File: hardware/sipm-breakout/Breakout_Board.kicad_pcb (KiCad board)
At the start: 2 copper layers, 14 parts, among them J1 Conn_02x34_Odd_Even, J10 Conn_Coaxial, J11 Conn_Coaxial, J12 Conn_Coaxial, J13 Conn_Coaxial, J14 Conn_Coaxial, J2 Conn_02x34_Odd_Even, J3 Conn_02x30_Odd_Even, J4 Conn_02x30_Odd_Even, J5 Conn_02x04_Top_Bottom, J6 Conn_01x04, J7 Conn_Coaxial, J8 Conn_Coaxial, J9 Conn_Coaxial

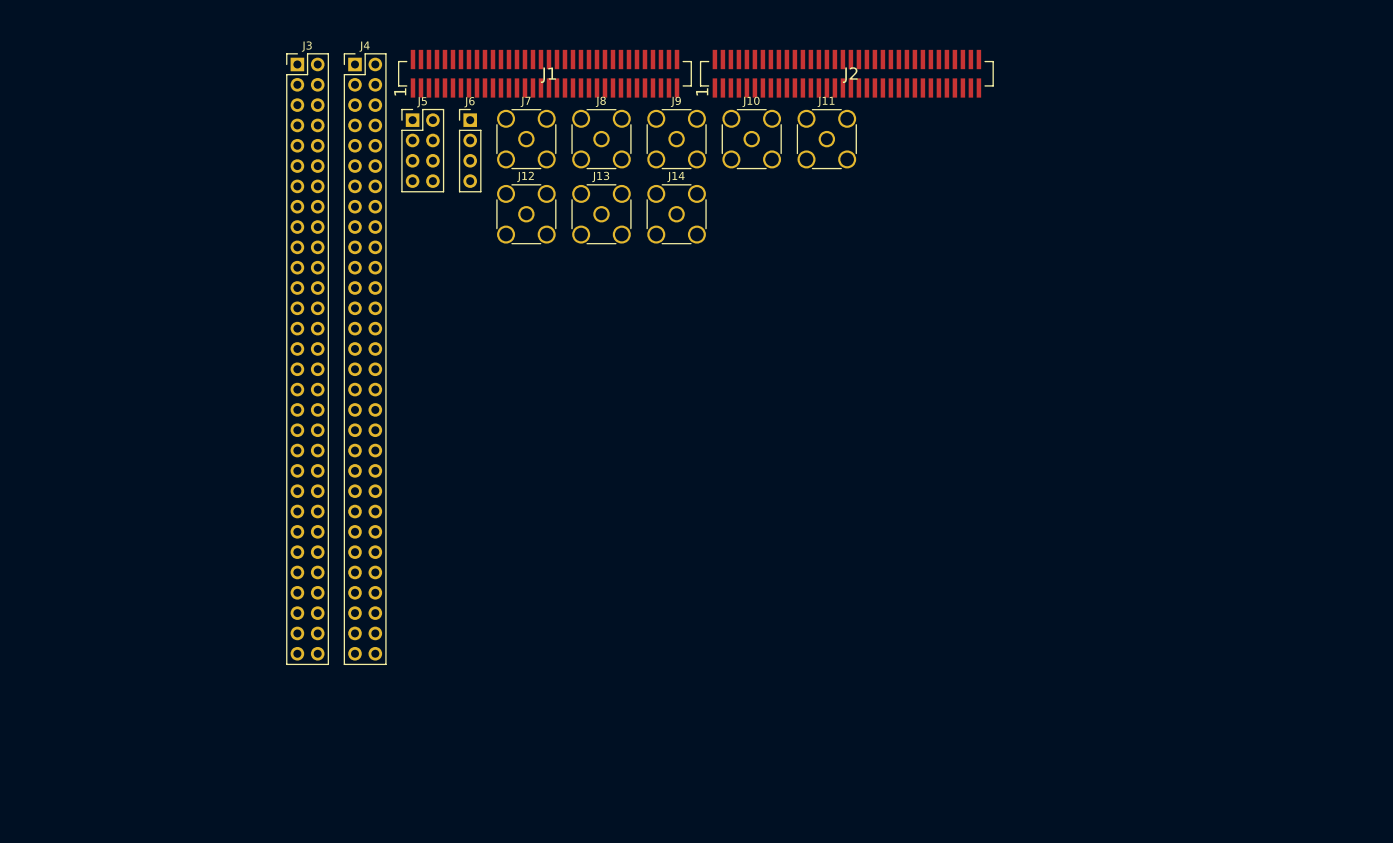
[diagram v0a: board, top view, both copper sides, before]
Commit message: add resistor packs, fix netlist
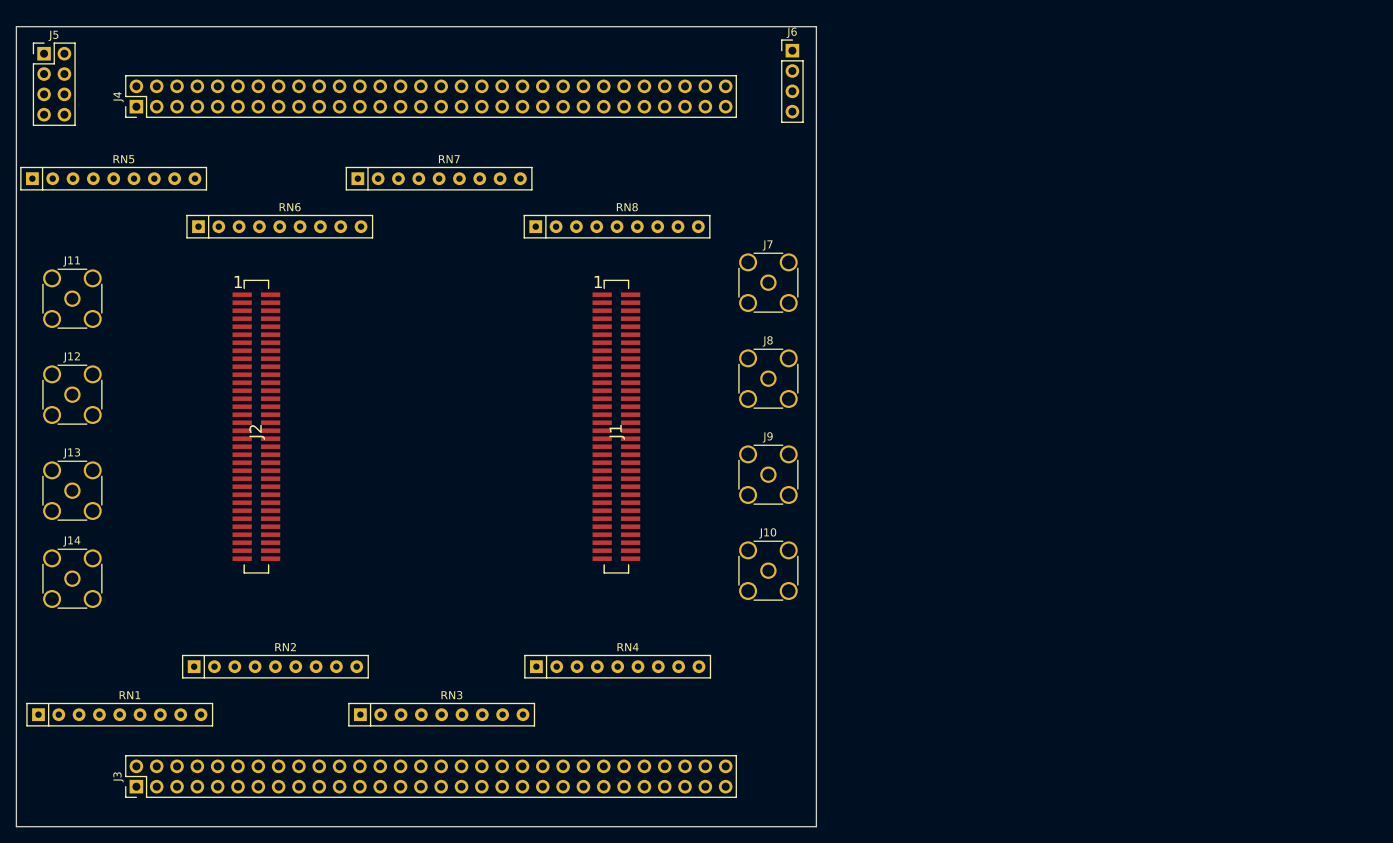
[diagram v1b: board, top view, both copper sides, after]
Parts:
- added RN1: R_Network08_US, Resistor_THT:R_Array_SIP9, F.Cu at (32.8, 111.0)
- added RN2: R_Network08_US, Resistor_THT:R_Array_SIP9, F.Cu at (52.2, 105.0)
- added RN3: R_Network08_US, Resistor_THT:R_Array_SIP9, F.Cu at (73.0, 111.0)
- added RN4: R_Network08_US, Resistor_THT:R_Array_SIP9, F.Cu at (95.0, 105.0)
- added RN5: R_Network08_US, Resistor_THT:R_Array_SIP9, F.Cu at (32.0, 44.0)
- added RN6: R_Network08_US, Resistor_THT:R_Array_SIP9, F.Cu at (52.8, 50.0)
- added RN7: R_Network08_US, Resistor_THT:R_Array_SIP9, F.Cu at (72.7, 44.0)
- added RN8: R_Network08_US, Resistor_THT:R_Array_SIP9, F.Cu at (94.9, 50.0)
- moved J11 96.4 mm to (37.0, 59.0)
- moved J3 92.5 mm to (45.0, 120.0), turned to 90 degrees
- moved J14 88.2 mm to (37.0, 94.0)
- moved J2 86.0 mm to (60.0, 75.0), turned to 270 degrees
- moved J13 74.6 mm to (37.0, 83.0)
- moved J12 61.1 mm to (37.0, 71.0)
- moved J10 54.0 mm to (124.0, 93.0)
- moved J5 46.8 mm to (33.5, 28.4)
- moved J1 45.0 mm to (105.0, 75.0), turned to 270 degrees
- moved J9 43.5 mm to (124.0, 81.0)
- moved J6 41.2 mm to (127.0, 28.0)
- moved J8 36.5 mm to (124.0, 69.0)
- moved J7 35.2 mm to (124.0, 57.0)
- moved J4 27.8 mm to (45.0, 35.0), turned to 90 degrees
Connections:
- J11 pad 1: /CH3 -> /BCH3
- J12 pad 1: /CH2 -> /BCH2
- J13 pad 1: /CH1 -> /BCH1
- J14 pad 1: /CH0 -> /BCH0
- J2 pad 1: /CH0 -> /BCH0
- J2 pad 11: /CH5 -> /BCH5
- J2 pad 13: /CH6 -> /BCH6
- J2 pad 15: /CH7 -> /BCH7
- J2 pad 17: /CH8 -> /BCH8
- J2 pad 19: /CH9 -> /BCH9
- J2 pad 21: /CH10 -> /BCH10
- J2 pad 23: /CH11 -> /BCH11
- J2 pad 25: /CH12 -> /BCH12
- J2 pad 27: /CH13 -> /BCH13
- J2 pad 29: /CH14 -> /BCH14
- J2 pad 3: /CH1 -> /BCH1
- J2 pad 31: /CH15 -> /BCH15
- J2 pad 33: /CH16 -> /BCH16
- J2 pad 35: /CH17 -> /BCH17
- J2 pad 37: /CH18 -> /BCH18
- J2 pad 39: /CH19 -> /BCH19
- J2 pad 41: /CH20 -> /BCH20
- J2 pad 43: /CH21 -> /BCH21
- J2 pad 45: /CH22 -> /BCH22
- J2 pad 47: /CH23 -> /BCH23
- J2 pad 49: /CH24 -> /BCH24
- J2 pad 5: /CH2 -> /BCH2
- J2 pad 51: /CH25 -> /BCH25
- J2 pad 53: /CH26 -> /BCH26
- J2 pad 55: /CH27 -> /BCH27
- J2 pad 57: /CH28 -> /BCH28
- J2 pad 59: /CH29 -> /BCH29
- J2 pad 61: /CH30 -> /BCH30
- J2 pad 63: /CH31 -> /BCH31
- J2 pad 7: /CH3 -> /BCH3
- J2 pad 9: /CH4 -> /BCH4
- J4 pad 1: /CH4 -> /BCH4
- J4 pad 11: /CH9 -> /BCH9
- J4 pad 13: /CH10 -> /BCH10
- J4 pad 15: /CH11 -> /BCH11
- J4 pad 17: /CH12 -> /BCH12
- J4 pad 19: /CH13 -> /BCH13
- J4 pad 21: /CH14 -> /BCH14
- J4 pad 23: /CH15 -> /BCH15
- J4 pad 25: /CH16 -> /BCH16
- J4 pad 27: /CH17 -> /BCH17
- J4 pad 29: /CH18 -> /BCH18
- J4 pad 3: /CH5 -> /BCH5
- J4 pad 31: /CH19 -> /BCH19
- J4 pad 33: /CH20 -> /BCH20
- J4 pad 35: /CH21 -> /BCH21
- J4 pad 37: /CH22 -> /BCH22
- J4 pad 39: /CH23 -> /BCH23
- J4 pad 41: /CH24 -> /BCH24
- J4 pad 43: /CH25 -> /BCH25
- J4 pad 45: /CH26 -> /BCH26
- J4 pad 47: /CH27 -> /BCH27
- J4 pad 49: /CH28 -> /BCH28
- J4 pad 5: /CH6 -> /BCH6
- J4 pad 51: /CH29 -> /BCH29
- J4 pad 53: /CH30 -> /BCH30
- J4 pad 55: /CH31 -> /BCH31
- J4 pad 7: /CH7 -> /BCH7
- J4 pad 9: /CH8 -> /BCH8
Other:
- board outline added: 100 x 100 mm

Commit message: partially routed
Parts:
- added H1: MountingHole_Pad, MountingHole:MountingHole_4.3mm_M4_Pad, F.Cu at (105.0, 30.0)
- added H2: MountingHole_Pad, MountingHole:MountingHole_4.3mm_M4_Pad, F.Cu at (105.0, 120.0)
- added H3: MountingHole_Pad, MountingHole:MountingHole_4.3mm_M4_Pad, F.Cu at (195.0, 30.0)
- added H4: MountingHole_Pad, MountingHole:MountingHole_4.3mm_M4_Pad, F.Cu at (195.0, 120.0)
- J1, J2: footprint Arich_SiPM_Footprints:MW-34-03-G-D-245-065-ES -> Breakout_Board_Parts:SAMTEC_CLM-134-02-F-D
- J10, J11, J12, J13, J14, J7, J8, J9: footprint Connector_Coaxial:SMA_Amphenol_132134_Vertical -> Breakout_Board_Parts:lemo-EPB.00.250.NTN
- J3, J4: value Conn_02x30_Odd_Even -> Conn_02x32_Odd_Even; footprint Connector_PinHeader_2.54mm:PinHeader_2x30_P2.54mm_Vertical -> Connector_PinHeader_2.00mm:PinHeader_2x32_P2.00mm_Vertical_SMD; moved to B.Cu
- RN1, RN2, RN3, RN4, RN5, RN6, RN7, RN8: footprint Resistor_THT:R_Array_SIP9 -> Breakout_Board_Parts:RPKG-9; moved to B.Cu
- moved J14 166.3 mm to (195.0, 42.0)
- moved J13 161.4 mm to (195.0, 50.0)
- moved J12 158.5 mm to (195.0, 58.0)
- moved J11 158.2 mm to (195.0, 66.0)
- moved RN5 154.1 mm to (186.0, 50.7), turned to 270 degrees
- moved J5 149.6 mm to (151.6, 120.1), turned to 90 degrees
- moved J4 137.0 mm to (176.0, 75.0), turned to 180 degrees
- moved RN6 134.3 mm to (186.0, 67.0), turned to 270 degrees
- moved RN7 119.8 mm to (186.0, 83.0), turned to 270 degrees
- moved J2 105.6 mm to (164.2, 58.0), turned to 90 degrees
- moved RN8 103.0 mm to (186.0, 98.0), turned to 270 degrees
- moved RN1 101.8 mm to (115.0, 51.0), turned to 270 degrees
- moved J6 92.0 mm to (122.1, 119.8), turned to 90 degrees
- moved J3 91.3 mm to (125.0, 76.0), turned to 180 degrees
- moved RN2 73.9 mm to (115.0, 66.0), turned to 270 degrees
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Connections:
- J3 pad 1: /CH4 -> /CH0
- J3 pad 11: /CH9 -> /CH5
- J3 pad 13: /CH10 -> /CH6
- J3 pad 15: /CH11 -> /CH7
- J3 pad 17: /CH12 -> /CH8
- J3 pad 19: /CH13 -> /CH9
- J3 pad 21: /CH14 -> /CH10
- J3 pad 23: /CH15 -> /CH11
- J3 pad 25: /CH16 -> /CH12
- J3 pad 27: /CH17 -> /CH13
- J3 pad 29: /CH18 -> /CH14
- J3 pad 3: /CH5 -> /CH1
- J3 pad 31: /CH19 -> /CH15
- J3 pad 33: /CH20 -> /CH16
- J3 pad 35: /CH21 -> /CH17
- J3 pad 37: /CH22 -> /CH18
- J3 pad 39: /CH23 -> /CH19
- J3 pad 41: /CH24 -> /CH20
- J3 pad 43: /CH25 -> /CH21
- J3 pad 45: /CH26 -> /CH22
- J3 pad 47: /CH27 -> /CH23
- J3 pad 49: /CH28 -> /CH24
- J3 pad 5: /CH6 -> /CH2
- J3 pad 51: /CH29 -> /CH25
- J3 pad 53: /CH30 -> /CH26
- J3 pad 55: /CH31 -> /CH27
- J3 pad 57: Net-(J3-Pad57) -> /CH28
- J3 pad 59: Net-(J3-Pad59) -> /CH29
- J3 pad 7: /CH7 -> /CH3
- J3 pad 9: /CH8 -> /CH4
- J4 pad 1: /BCH4 -> /BCH0
- J4 pad 11: /BCH9 -> /BCH5
- J4 pad 13: /BCH10 -> /BCH6
- J4 pad 15: /BCH11 -> /BCH7
- J4 pad 17: /BCH12 -> /BCH8
- J4 pad 19: /BCH13 -> /BCH9
- J4 pad 21: /BCH14 -> /BCH10
- J4 pad 23: /BCH15 -> /BCH11
- J4 pad 25: /BCH16 -> /BCH12
- J4 pad 27: /BCH17 -> /BCH13
- J4 pad 29: /BCH18 -> /BCH14
- J4 pad 3: /BCH5 -> /BCH1
- J4 pad 31: /BCH19 -> /BCH15
- J4 pad 33: /BCH20 -> /BCH16
- J4 pad 35: /BCH21 -> /BCH17
- J4 pad 37: /BCH22 -> /BCH18
- J4 pad 39: /BCH23 -> /BCH19
- J4 pad 41: /BCH24 -> /BCH20
- J4 pad 43: /BCH25 -> /BCH21
- J4 pad 45: /BCH26 -> /BCH22
- J4 pad 47: /BCH27 -> /BCH23
- J4 pad 49: /BCH28 -> /BCH24
- J4 pad 5: /BCH6 -> /BCH2
- J4 pad 51: /BCH29 -> /BCH25
- J4 pad 53: /BCH30 -> /BCH26
- J4 pad 55: /BCH31 -> /BCH27
- J4 pad 57: Net-(J4-Pad57) -> /BCH28
- J4 pad 59: Net-(J4-Pad59) -> /BCH29
- J4 pad 7: /BCH7 -> /BCH3
- J4 pad 9: /BCH8 -> /BCH4
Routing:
- net GND: track 0.00 -> 83.8 mm, vias 0 -> 43
- net /CH3: track 0.00 -> 55.1 mm, vias 0 -> 1
- net /CH2: track 0.00 -> 48.3 mm, vias 0 -> 1
- net /CH0: track 0.00 -> 47.7 mm, vias 0 -> 1
- net /CH1: track 0.00 -> 43.5 mm, vias 0 -> 1
- net /CH23: track 0.00 -> 31.5 mm, vias 0 -> 1
- net /CH4: track 0.00 -> 31.2 mm, vias 0 -> 1
- net /CH5: track 0.00 -> 31.0 mm, vias 0 -> 1
- net /CH6: track 0.00 -> 30.1 mm, vias 0 -> 1
- net /CH22: track 0.00 -> 29.9 mm, vias 0 -> 1
- net /CH7: track 0.00 -> 28.6 mm, vias 0 -> 1
- net /CH31: track 0.00 -> 28.0 mm, vias 0 -> 1
- net /CH20: track 0.00 -> 28.0 mm, vias 0 -> 1
- net /CH15: track 0.00 -> 27.7 mm, vias 0 -> 1
- net /BCH0: track 0.00 -> 27.5 mm, vias 0 -> 1
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- added copper zone on F.Cu, net GND
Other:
- net class Default: clearance 0.2 -> 0.1778; trace_width 0.25 -> 0.1778; via_dia 0.8 -> 0.635; via_drill 0.4 -> 0.3048
- rule pad_to_mask_clearance: 0 -> 0.0381
- rule trace_clearance: 0.2 -> 0.1778
- rule trace_min: 0.2 -> 0.1778
- rule via_min_drill: 0.3 -> 0.2032
- rule via_min_size: 0.4 -> 0.635

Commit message: Possibly final break board
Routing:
- net /BIAS1: track 0.00 -> 82.5 mm, vias 0 -> 4
- net /BIAS3: track 0.00 -> 71.3 mm, vias 0 -> 4
- net GND: track 83.8 -> 135.5 mm, vias 43 -> 71
- net /VDD: track 0.00 -> 47.4 mm, vias 0 -> 1
- net /BCH31: track 0.00 -> 41.9 mm, vias 0 -> 1
- net /OUT: track 0.00 -> 41.2 mm, vias 0 -> 1
- net /BCH30: track 0.00 -> 41.0 mm, vias 0 -> 1
- net /BCH29: track 0.00 -> 39.2 mm, vias 0 -> 1
- net /BCH28: track 0.00 -> 38.5 mm, vias 0 -> 1
- net /BIAS2: track 0.00 -> 37.2 mm, vias 0 -> 1
- net /BCH27: track 0.00 -> 37.2 mm, vias 0 -> 1
- net /BCH26: track 0.00 -> 35.7 mm, vias 0 -> 1
- net /BCH25: track 0.00 -> 34.9 mm, vias 0 -> 1
- net /BCH24: track 0.00 -> 34.4 mm, vias 0 -> 1
- net /BIAS4: track 0.00 -> 33.7 mm
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- added copper zone on B.Cu, net GND
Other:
- board text added: "EMPHATIC SiPM Breakout Rev A -- 2021-03 ESH http://edf.bu.edu"
- board text added: "UP"

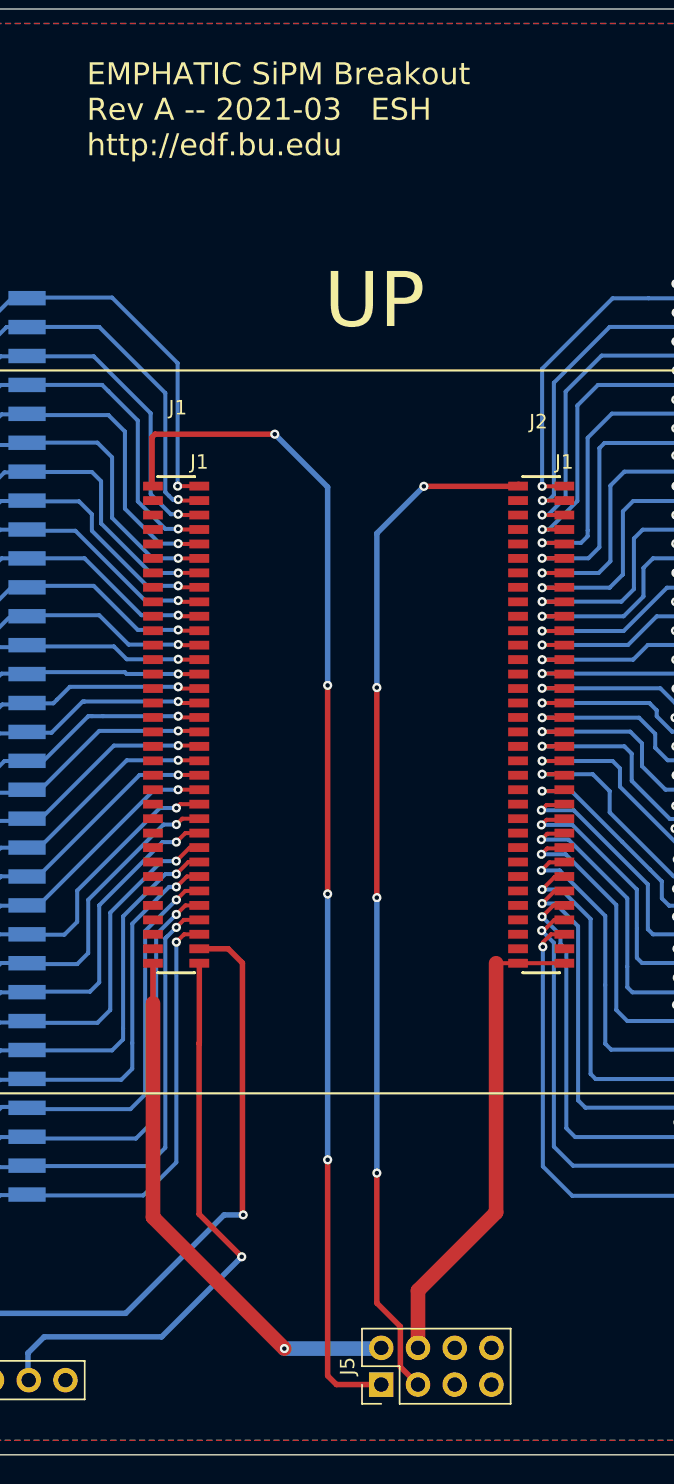
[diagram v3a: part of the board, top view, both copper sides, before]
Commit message: Rev B breakout board
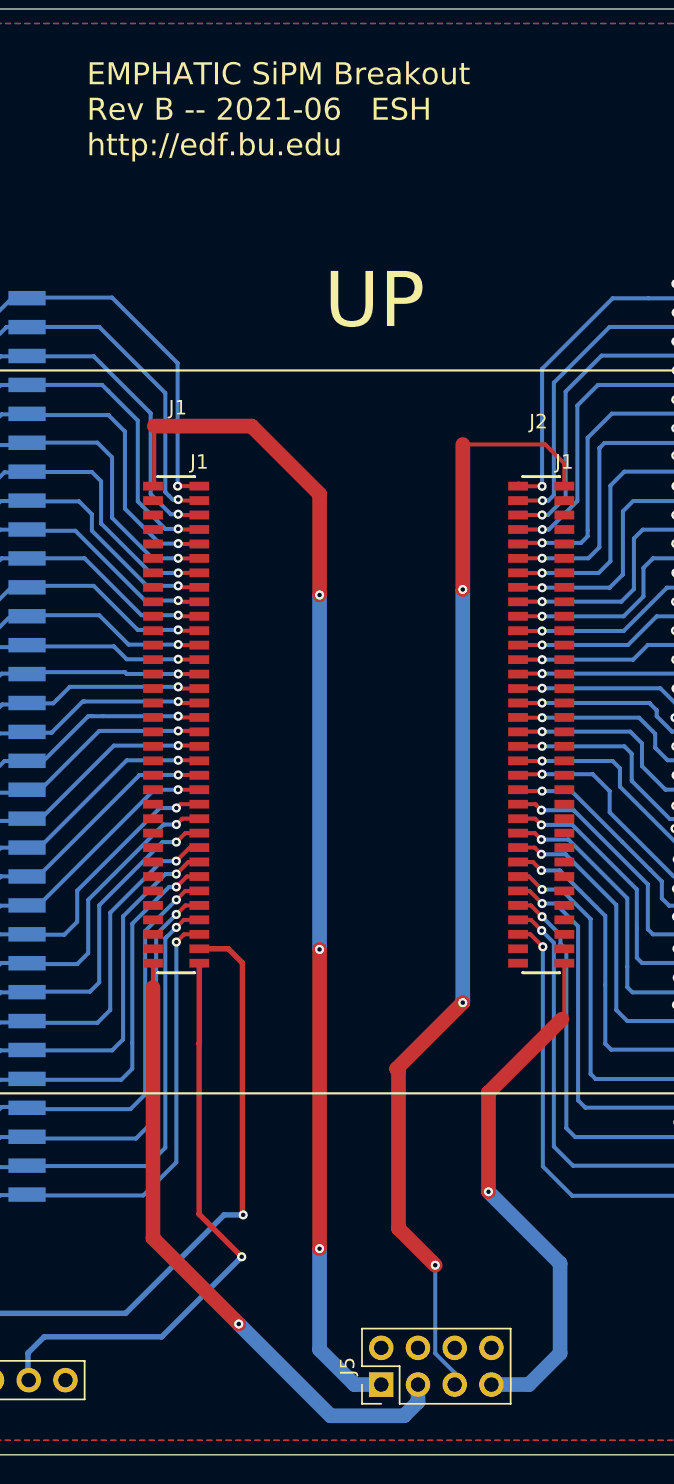
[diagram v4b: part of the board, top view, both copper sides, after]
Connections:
- J2 pad 1: /BCH0 -> /BIAS3
- J2 pad 10: GND -> /BCH4
- J2 pad 11: /BCH5 -> GND
- J2 pad 12: GND -> /BCH5
- J2 pad 13: /BCH6 -> GND
- J2 pad 14: GND -> /BCH6
- J2 pad 15: /BCH7 -> GND
- J2 pad 16: GND -> /BCH7
- J2 pad 17: /BCH8 -> GND
- J2 pad 18: GND -> /BCH8
- J2 pad 19: /BCH9 -> GND
- J2 pad 2: /BIAS3 -> /BCH0
- J2 pad 20: GND -> /BCH9
- J2 pad 21: /BCH10 -> GND
- J2 pad 22: GND -> /BCH10
- J2 pad 23: /BCH11 -> GND
- J2 pad 24: GND -> /BCH11
- J2 pad 25: /BCH12 -> GND
- J2 pad 26: GND -> /BCH12
- J2 pad 27: /BCH13 -> GND
- J2 pad 28: GND -> /BCH13
- J2 pad 29: /BCH14 -> GND
- J2 pad 3: /BCH1 -> GND
- J2 pad 30: GND -> /BCH14
- J2 pad 31: /BCH15 -> GND
- J2 pad 32: GND -> /BCH15
- J2 pad 33: /BCH16 -> GND
- J2 pad 34: GND -> /BCH16
- J2 pad 35: /BCH17 -> GND
- J2 pad 36: GND -> /BCH17
- J2 pad 37: /BCH18 -> GND
- J2 pad 38: GND -> /BCH18
- J2 pad 39: /BCH19 -> GND
- J2 pad 4: GND -> /BCH1
- J2 pad 40: GND -> /BCH19
- J2 pad 41: /BCH20 -> GND
- J2 pad 42: GND -> /BCH20
- J2 pad 43: /BCH21 -> GND
- J2 pad 44: GND -> /BCH21
- J2 pad 45: /BCH22 -> GND
- J2 pad 46: GND -> /BCH22
- J2 pad 47: /BCH23 -> GND
- J2 pad 48: GND -> /BCH23
- J2 pad 49: /BCH24 -> GND
- J2 pad 5: /BCH2 -> GND
- J2 pad 50: GND -> /BCH24
- J2 pad 51: /BCH25 -> GND
- J2 pad 52: GND -> /BCH25
- J2 pad 53: /BCH26 -> GND
- J2 pad 54: GND -> /BCH26
- J2 pad 55: /BCH27 -> GND
- J2 pad 56: GND -> /BCH27
- J2 pad 57: /BCH28 -> GND
- J2 pad 58: GND -> /BCH28
- J2 pad 59: /BCH29 -> GND
- J2 pad 6: GND -> /BCH2
- J2 pad 60: GND -> /BCH29
- J2 pad 61: /BCH30 -> GND
- J2 pad 62: GND -> /BCH30
- J2 pad 63: /BCH31 -> GND
- J2 pad 64: GND -> /BCH31
- J2 pad 65: Net-(J2-Pad65) -> GND
- J2 pad 66: GND -> Net-(J2-Pad66)
- J2 pad 68: /BIAS4 -> Net-(J2-Pad68)
- J2 pad 7: /BCH3 -> GND
- J2 pad 8: GND -> /BCH3
- J2 pad 9: /BCH4 -> GND
- J5 pad 2: /BIAS2 -> GND
- J5 pad 3: /BIAS3 -> /BIAS2
- J5 pad 4: /BIAS4 -> GND
- J5 pad 5: GND -> /BIAS3
- J5 pad 7: GND -> /BIAS4
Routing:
- net /BIAS2: track 37.2 -> 44.0 mm
- net /BIAS3: track 71.3 -> 77.7 mm, vias 4 -> 3
- net /BIAS4: track 33.7 -> 36.9 mm, vias 0 -> 1
- net GND: track 135.5 -> 136.4 mm
- net /BIAS1: track 82.5 -> 82.0 mm, vias 4 -> 3
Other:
- board text added: "EMPHATIC SiPM Breakout Rev B -- 2021-06 ESH http://edf.bu.edu"
- board text removed: "EMPHATIC SiPM Breakout Rev A -- 2021-03 ESH http://edf.bu.edu"
